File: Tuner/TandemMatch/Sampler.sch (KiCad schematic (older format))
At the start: 56 parts, among them J42 Conn_Coaxial, J43 Conn_Coaxial, J44 Conn_01x01, J45 Conn_01x01, J46 Conn_01x01, J47 Conn_01x01, J48 Conn_01x01, J49 Conn_01x01, J50 Conn_01x01, J51 Conn_01x01, J52 Conn_01x01, J53 Conn_01x01, J54 Conn_01x01, J55 Conn_01x01, J56 Conn_01x01, J57 Conn_01x01, J58 Conn_01x01, J59 Conn_01x01, J60 Conn_Coaxial, J61 Conn_Coaxial, J62 Conn_01x04, J63 Conn_01x01, J64 Conn_01x01, J65 Conn_01x01, J66 Conn_01x01

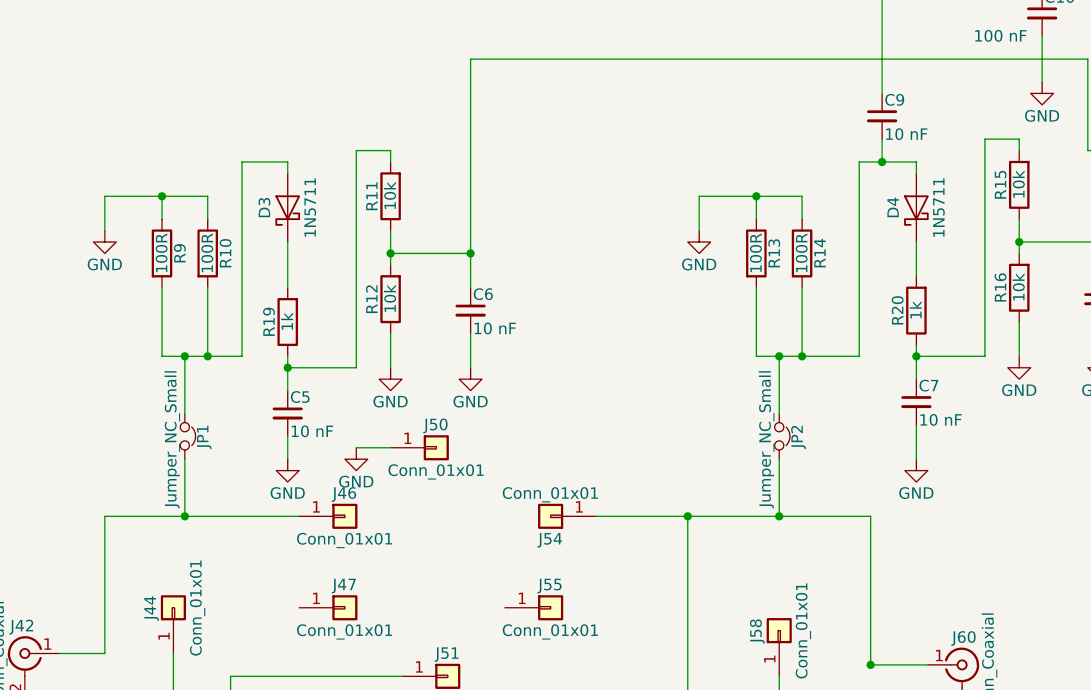
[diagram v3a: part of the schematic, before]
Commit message: Removed 1k resistors, did some more rearranging on TandemMatch
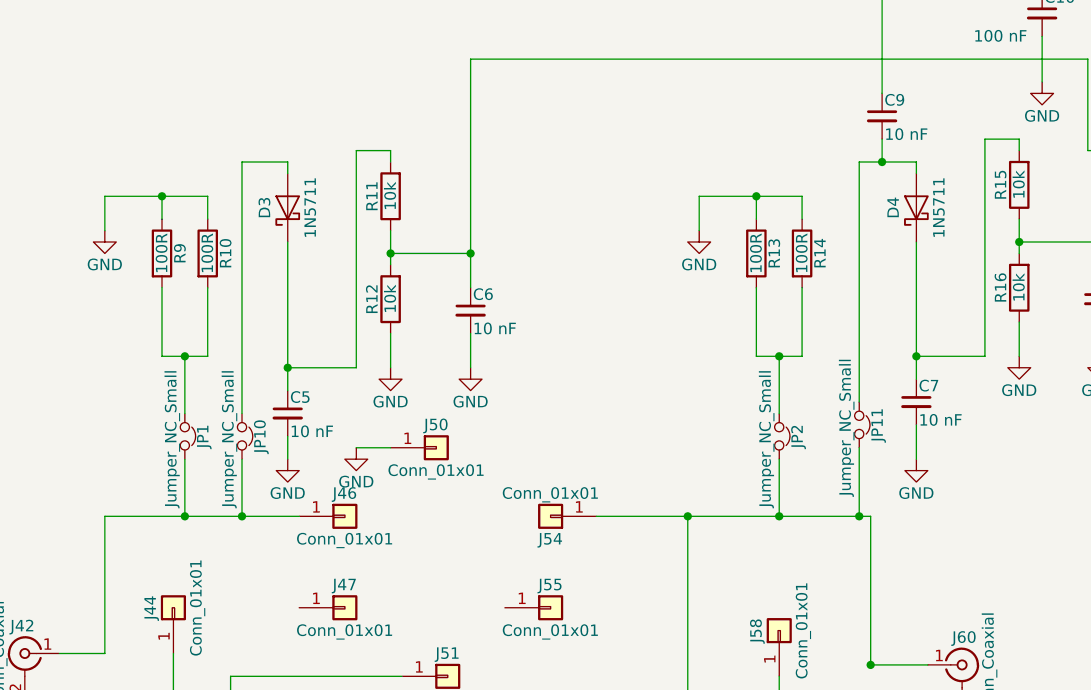
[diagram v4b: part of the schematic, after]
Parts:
- removed R19, R20: 1k, Resistors_THT:R_Axial_DIN0207_L6.3mm_D2.5mm_P7.62mm_Horizontal, symbol R
- added JP10, JP11: Jumper_NC_Small, Pin_Headers:Pin_Header_Straight_1x02_Pitch2.54mm, symbol Jumper_NC_Small
- R10, R13, R14, R9: footprint Resistors_THT:R_Axial_DIN0207_L6.3mm_D2.5mm_P7.62mm_Horizontal -> TandemMatch:R_Axial_DIN0207_L6.3mm_D2.5mm_P7.62mm_Horizontal_SMD
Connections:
- net at J42.1 (In), J46.1 (Pin_1), JP1.2: now also JP10.2
- net at J52.1 (Pin_1), J54.1 (Pin_1), J60.1 (In)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: now also JP11.2
- net at JP1.1, R10.2, R9.2: no longer D3.2 (A)
- net at JP2.1, R13.2, R14.2: no longer C9.2, D4.2 (A)
- net at D3.1 (K): now also C5.1, R11.2
- net at D4.1 (K): now also C7.1, R15.2
- new net: D3.2 (A), JP10.1
- new net: C9.2, D4.2 (A), JP11.1
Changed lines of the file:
@@
 F 0 "R9" V 2730 2150 50  0000 C CNN
 F 1 "100R" V 2650 2150 50  0000 C CNN
-F 2 "Resistors_THT:R_Axial_DIN0207_L6.3mm_D2.5mm_P7.62mm_Horizontal" V 2580 2150 50  0001 C CNN
+F 2 "TandemMatch:R_Axial_DIN0207_L6.3mm_D2.5mm_P7.62mm_Horizontal_SMD" V 2580 2150 50  0001 C CNN
 F 3 "" H 2650 2150 50  0001 C CNN
 	1    2650 2150
@@
 F 0 "R10" V 2930 2150 50  0000 C CNN
 F 1 "100R" V 2850 2150 50  0000 C CNN
-F 2 "Resistors_THT:R_Axial_DIN0207_L6.3mm_D2.5mm_P7.62mm_Horizontal" V 2780 2150 50  0001 C CNN
+F 2 "TandemMatch:R_Axial_DIN0207_L6.3mm_D2.5mm_P7.62mm_Horizontal_SMD" V 2780 2150 50  0001 C CNN
 F 3 "" H 2850 2150 50  0001 C CNN
 	1    2850 2150
@@
 F 0 "R13" V 5330 2150 50  0000 C CNN
 F 1 "100R" V 5250 2150 50  0000 C CNN
-F 2 "Resistors_THT:R_Axial_DIN0207_L6.3mm_D2.5mm_P7.62mm_Horizontal" V 5180 2150 50  0001 C CNN
+F 2 "TandemMatch:R_Axial_DIN0207_L6.3mm_D2.5mm_P7.62mm_Horizontal_SMD" V 5180 2150 50  0001 C CNN
 F 3 "" H 5250 2150 50  0001 C CNN
 	1    5250 2150
@@
 F 0 "R14" V 5530 2150 50  0000 C CNN
 F 1 "100R" V 5450 2150 50  0000 C CNN
-F 2 "Resistors_THT:R_Axial_DIN0207_L6.3mm_D2.5mm_P7.62mm_Horizontal" V 5380 2150 50  0001 C CNN
+F 2 "TandemMatch:R_Axial_DIN0207_L6.3mm_D2.5mm_P7.62mm_Horizontal_SMD" V 5380 2150 50  0001 C CNN
 F 3 "" H 5450 2150 50  0001 C CNN
 	1    5450 2150
@@
 Wire Wire Line
 	2750 2850 2750 2600
-Connection ~ 5450 2600
-Wire Wire Line
-	5250 2600 5700 2600
-Wire Wire Line
-	5700 2600 5700 1750
+Wire Wire Line
+	5250 2600 5450 2600
+Wire Wire Line
+	5700 1750 5700 2800
 Wire Wire Line
 	5700 1750 5950 1750
-Connection ~ 2850 2600
 Wire Wire Line
 	3200 1750 3200 1800
@@
 	3000 1750 3200 1750
 Wire Wire Line
-	3000 2600 3000 1750
-Wire Wire Line
-	2650 2600 3000 2600
+	3000 1750 3000 2850
+Wire Wire Line
+	2650 2600 2850 2600
 Connection ~ 5750 5450
 Wire Wire Line
@@
 	6400 2600 6400 2450
 Wire Wire Line
-	5950 2100 5950 2250
+	5950 2100 5950 2700
 Connection ~ 3650 2150
 Wire Wire Line
@@
 	3650 2650 3650 2500
 Wire Wire Line
-	3200 2100 3200 2300
+	3200 2100 3200 2750
 Wire Wire Line
 	5250 2300 5250 2600
@@
 	7000 1000 7000 900
 Connection ~ 7000 900
-$Comp
-L R R19
-U 1 1 5C75CDD1
-P 3200 2450
-F 0 "R19" V 3280 2450 50  0000 C CNN
-F 1 "1k" V 3200 2450 50  0000 C CNN
-F 2 "Resistors_THT:R_Axial_DIN0207_L6.3mm_D2.5mm_P7.62mm_Horizontal" V 3130 2450 50  0001 C CNN
-F 3 "" H 3200 2450 50  0001 C CNN
-	1    3200 2450
-	-1   0    0    1
-$EndComp
 Wire Wire Line
 	3200 2950 3200 3050
-$Comp
-L R R20
-U 1 1 5C75D36D
-P 5950 2400
-F 0 "R20" V 6030 2400 50  0000 C CNN
-F 1 "1k" V 5950 2400 50  0000 C CNN
-F 2 "Resistors_THT:R_Axial_DIN0207_L6.3mm_D2.5mm_P7.62mm_Horizontal" V 5880 2400 50  0001 C CNN
-F 3 "" H 5950 2400 50  0001 C CNN
-	1    5950 2400
-	-1   0    0    1
-$EndComp
 Wire Wire Line
 	5950 2900 5950 3050
-Wire Wire Line
-	3200 2600 3200 2750
 Wire Wire Line
 	3500 2650 3200 2650
 Connection ~ 3200 2650
-Wire Wire Line
-	5950 2550 5950 2700
 Wire Wire Line
 	6250 2600 5950 2600
@@
 Wire Wire Line
 	2700 7450 2700 7400
+$Comp
+L Jumper_NC_Small JP10
+U 1 1 5C779F52
+P 3000 2950
+F 0 "JP10" H 3000 3030 50  0000 C CNN
+F 1 "Jumper_NC_Small" H 3010 2890 50  0000 C CNN
+F 2 "Pin_Headers:Pin_Header_Straight_1x02_Pitch2.54mm" H 3000 2950 50  0001 C CNN
+F 3 "" H 3000 2950 50  0001 C CNN
+	1    3000 2950
+	0    1    1    0
+$EndComp
+Wire Wire Line
+	3000 3050 3000 3300
+Connection ~ 3000 3300
+$Comp
+L Jumper_NC_Small JP11
+U 1 1 5C77A385
+P 5700 2900
+F 0 "JP11" H 5700 2980 50  0000 C CNN
+F 1 "Jumper_NC_Small" H 5710 2840 50  0000 C CNN
+F 2 "Pin_Headers:Pin_Header_Straight_1x02_Pitch2.54mm" H 5700 2900 50  0001 C CNN
+F 3 "" H 5700 2900 50  0001 C CNN
+	1    5700 2900
+	0    1    1    0
+$EndComp
+Wire Wire Line
+	5700 3000 5700 3300
+Connection ~ 5700 3300
 $EndSCHEMATC
